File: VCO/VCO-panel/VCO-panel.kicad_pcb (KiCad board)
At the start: 2 copper layers, 20 x 128.5 mm, 0 parts

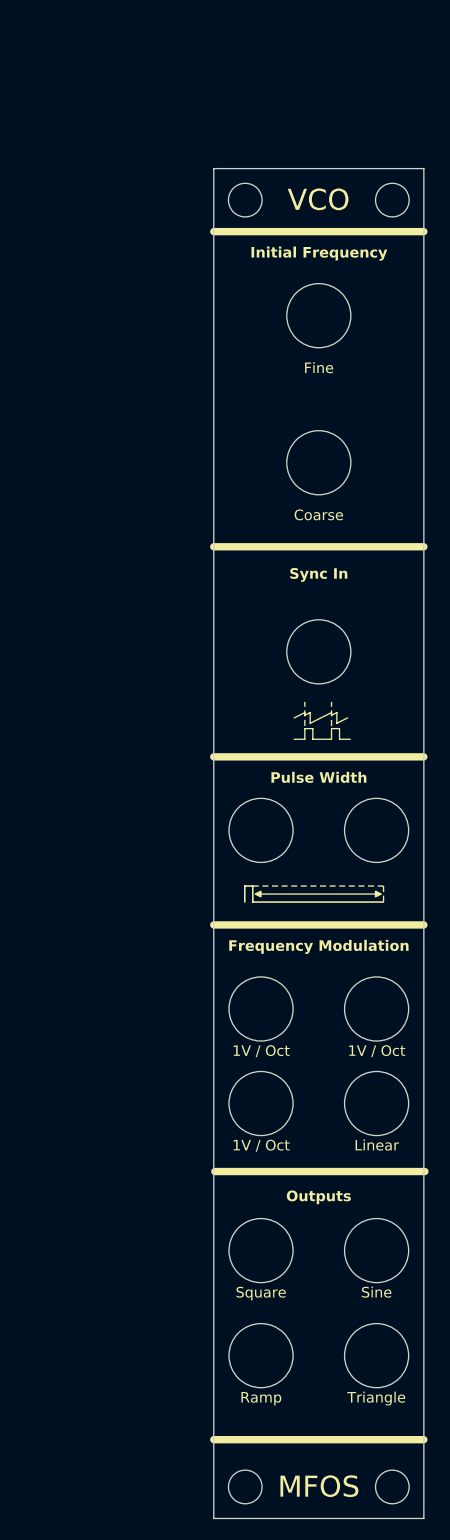
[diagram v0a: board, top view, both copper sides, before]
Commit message: split VCO controls plane in separate project
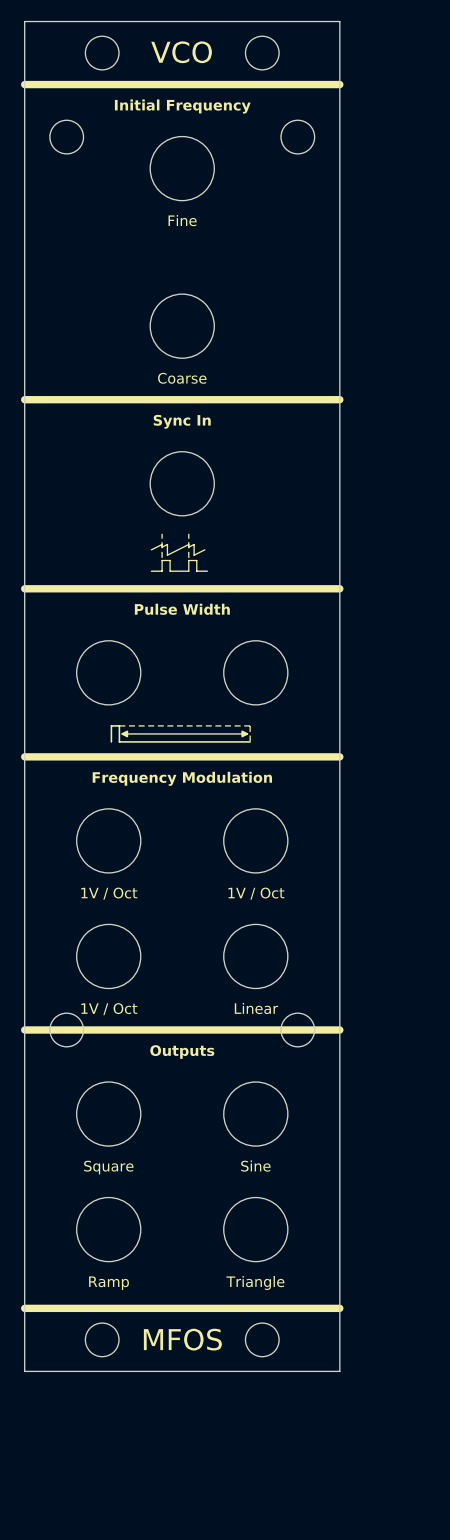
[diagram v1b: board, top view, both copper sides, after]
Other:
- board size 20 x 128.5 mm -> 30 x 128.5 mm
